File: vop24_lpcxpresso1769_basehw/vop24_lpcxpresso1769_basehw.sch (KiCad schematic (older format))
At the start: 10 parts, among them J1 Micro_SD_Card, J2 Conn_01x05_Male, J3 Conn_01x06_Male, U1 LPCXpresso1769

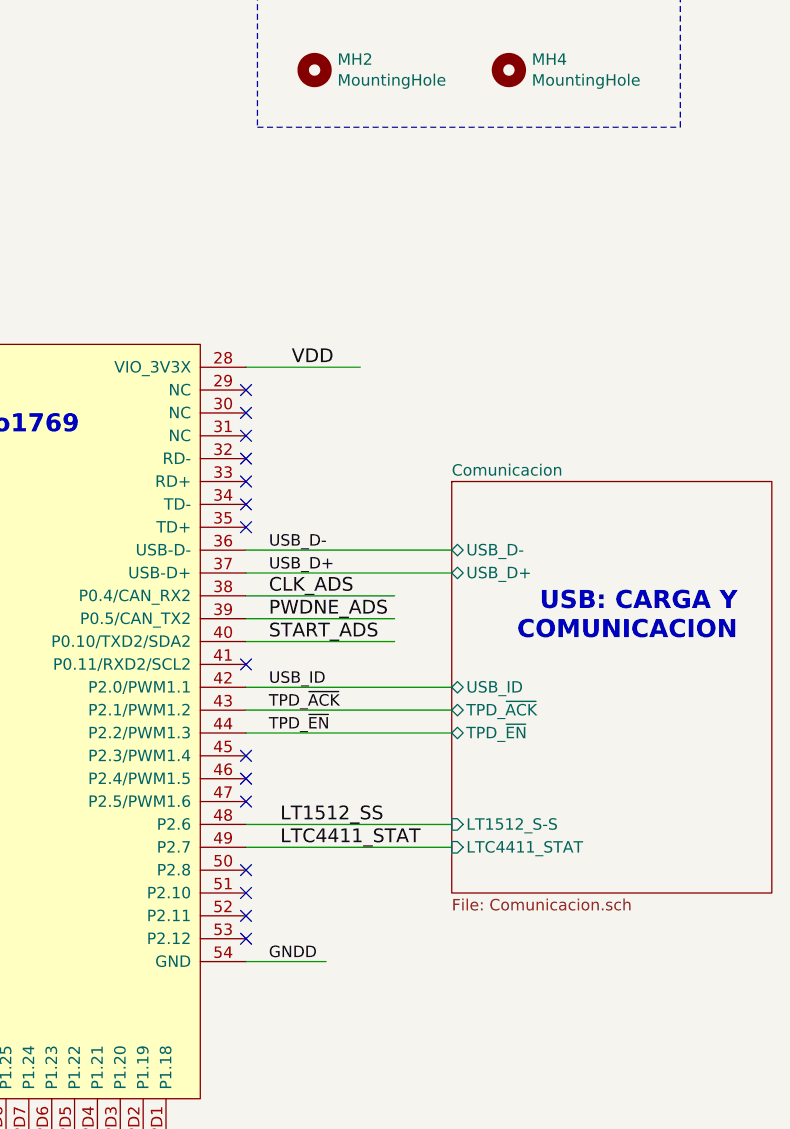
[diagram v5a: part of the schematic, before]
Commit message: ESQ: cambios menores PCB: finalizacion de ruteo con 0.3mm. Previo a poligonos
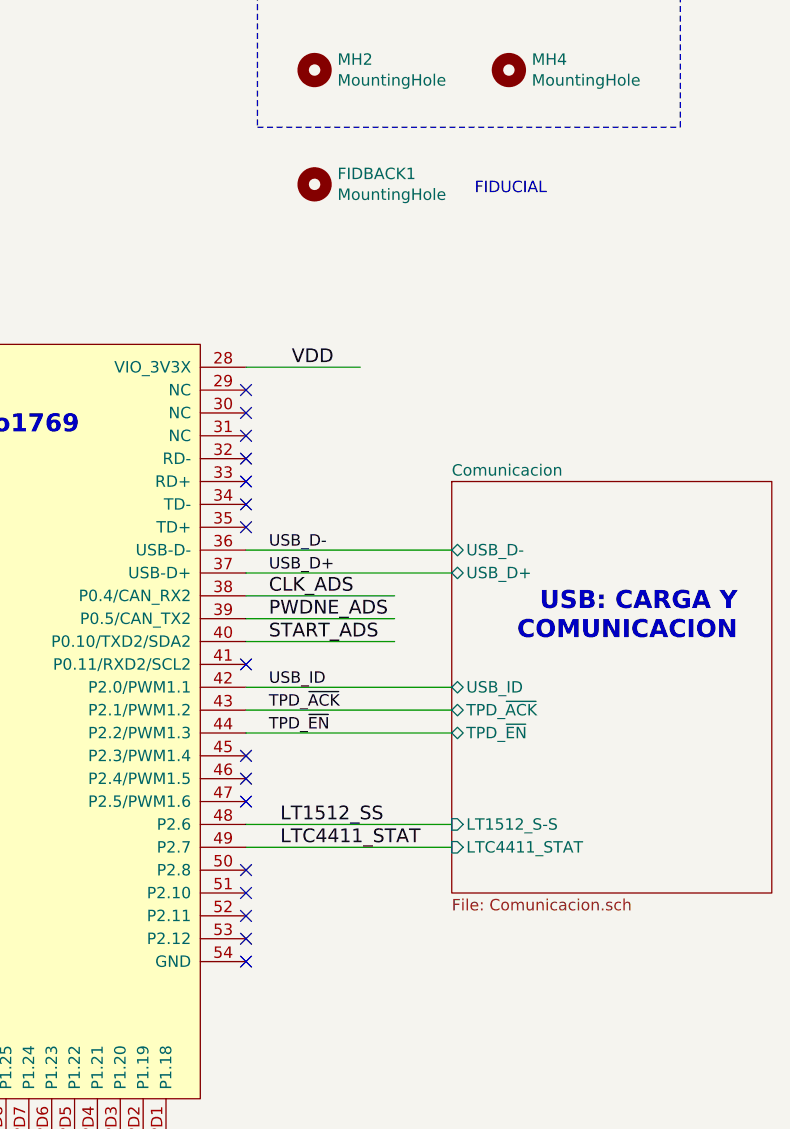
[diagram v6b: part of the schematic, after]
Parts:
- added FIDBACK1: MountingHole, Fiducial:Fiducial_0.75mm_Dia_1.5mm_Outer, symbol Mechanical:MountingHole
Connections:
- wire segments 70 -> 69
- no-connect marks 43 -> 44
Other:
- note added: "FIDUCIAL"
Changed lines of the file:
@@
 Text Label 1500 6000 2    60   ~ 0
-GNDD
-Wire Wire Line
-	8050 5350 8400 5350
-Text Label 8150 5350 0    50   ~ 0
 GNDD
 Text Label 8200 4750 0    60   ~ 0
@@
 Text Notes 8300 850  0    50   ~ 0
 Agujeros de sujeción
+NoConn ~ 8050 5350
+Text Notes 9050 2000 0    50   ~ 0
+FIDUCIAL
+$Comp
+L Mechanical:MountingHole FIDBACK1
+U 1 1 5BFF8AF2
+P 8350 1950
+F 0 "FIDBACK1" H 8450 1996 50  0000 L CNN
+F 1 "MountingHole" H 8450 1905 50  0000 L CNN
+F 2 "Fiducial:Fiducial_0.75mm_Dia_1.5mm_Outer" H 8350 1950 50  0001 C CNN
+F 3 "~" H 8350 1950 50  0001 C CNN
+	1    8350 1950
+	1    0    0    -1
+$EndComp
 $EndSCHEMATC
